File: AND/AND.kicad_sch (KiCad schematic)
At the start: 7 parts, among them J1 AudioJack2_SwitchT, J2 AudioJack2_SwitchT, J3 AudioJack2_SwitchT, Q1 2N7002, Q2 BSS84, Q3 BSS84

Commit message: Increase impedance
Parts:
- R1: value 100k -> 1M
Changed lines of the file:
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@@
       (effects (font (size 1.27 1.27)) (justify left))
     )
-    (property "Value" "100k" (at 81.153 76.7771 0)
+    (property "Value" "1M" (at 81.153 76.7771 0)
       (effects (font (size 1.27 1.27)) (justify left))
     )

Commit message: Layout AND gate
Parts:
- J1, J2, J3: footprint (none) -> Custom_FP:PJ398SM
- R1: footprint (none) -> Resistor_SMD:R_0603_1608Metric
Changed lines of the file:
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@@
 			)
 		)
-		(property "Footprint" ""
+		(property "Footprint" "Custom_FP:PJ398SM"
 			(at 66.04 90.17 0)
 			(effects
@@
 			)
 		)
-		(property "Footprint" ""
+		(property "Footprint" "Custom_FP:PJ398SM"
 			(at 120.65 70.485 0)
 			(effects
@@
 			)
 		)
-		(property "Footprint" ""
+		(property "Footprint" "Resistor_SMD:R_0603_1608Metric"
 			(at 77.597 75.565 90)
 			(effects
@@
 			)
 		)
-		(property "Footprint" ""
+		(property "Footprint" "Custom_FP:PJ398SM"
 			(at 63.5 70.485 0)
 			(effects

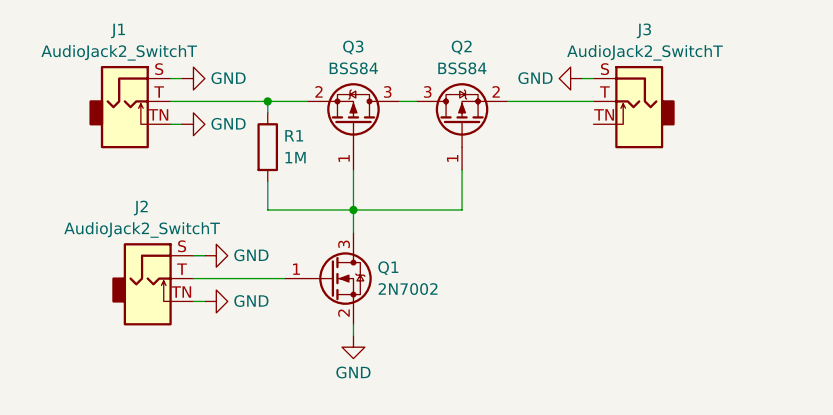
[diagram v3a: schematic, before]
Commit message: Improve AND gate off state
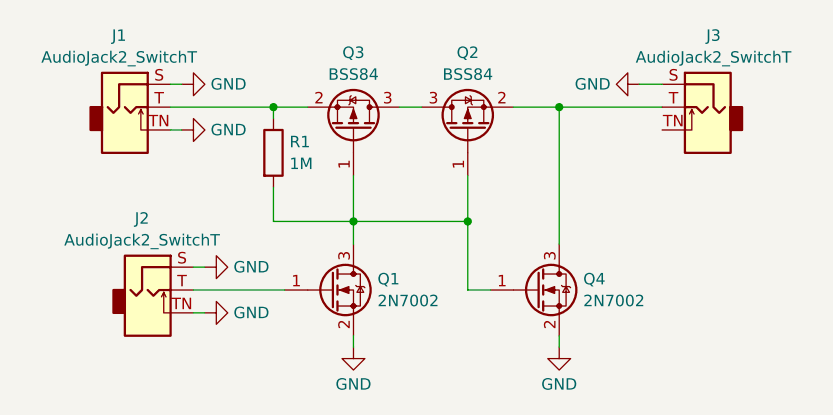
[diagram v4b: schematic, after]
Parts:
- added Q4: 2N7002, Package_TO_SOT_SMD:SOT-23, symbol Transistor_FET:2N7002
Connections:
- net GND: now also Q4.2 (S)
- net at Q1.3 (D), Q2.1 (G), Q3.1 (G)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: now also Q4.1 (G)
- net at J3.T, Q2.2 (S): now also Q4.3 (D)
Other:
- moved on the sheet: J1, J2, J3, Q1, Q2, Q3, R1
